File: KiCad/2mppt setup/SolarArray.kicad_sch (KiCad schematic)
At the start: 4 parts

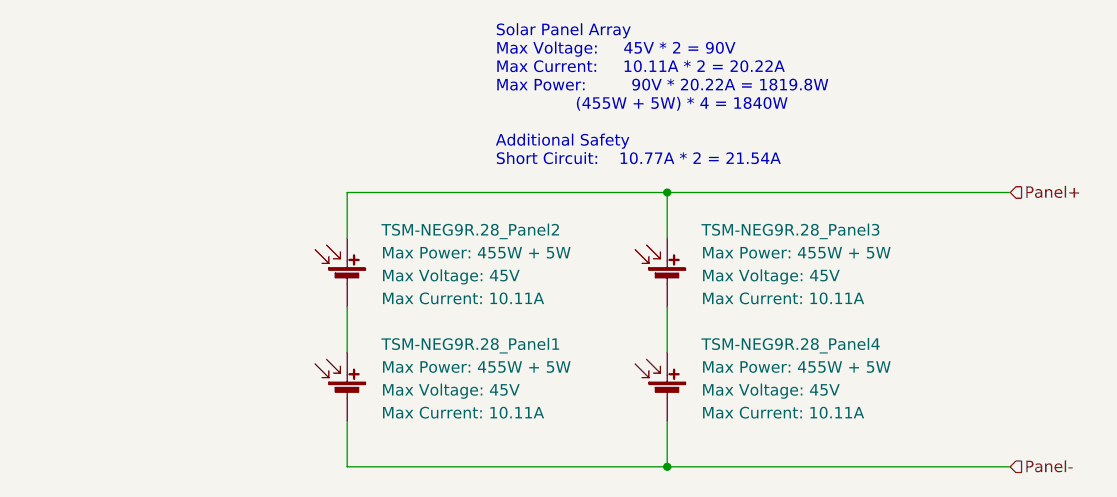
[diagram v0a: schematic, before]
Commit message: exclude text from sim
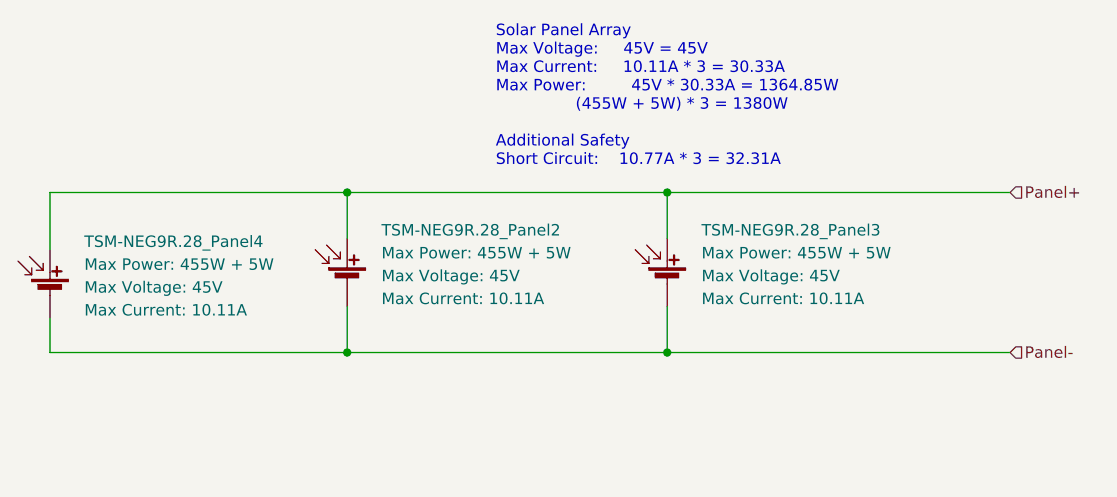
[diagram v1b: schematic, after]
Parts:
- removed TSM-NEG9R.28_Panel1: 455W, symbol Proa:Solar_Cell
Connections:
- net Panel+: now also TSM-NEG9R.28_Panel4.1 (+)
- net Panel-: now also TSM-NEG9R.28_Panel2.2 (-), TSM-NEG9R.28_Panel3.2 (-)
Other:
- note added: "Solar Panel Array Max Voltage: 45V = 45V Max Current: 10.11A * 3 = 30.33A Max Power: 45V * 30.33A = 1364.85W (455W + 5W) * 3 = 1380W Additional Safety Short Circuit: 10.77A * 3 = 32.31A"
- note removed: "Solar Panel Array Max Voltage: 45V * 2 = 90V Max Current: 10.11A * 2 = 20.22A Max Power: 90V * 20.22A = 1819.8W (455W + 5W) * 4 = 1840W Additional Safety Short Circuit: 10.77A * 2 = 21.54A"
- moved on the sheet: TSM-NEG9R.28_Panel4
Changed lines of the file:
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@@
 	(generator_version "9.0")
 	(paper "A4")
-	(text "Solar Panel Array\nMax Voltage: 	45V * 2 = 90V\nMax Current: 	10.11A * 2 = 20.22A\nMax Power: 		90V * 20.22A = 1819.8W\n				(455W + 5W) * 4 = 1840W\n\nAdditional Safety\nShort Circuit:	10.77A * 2 = 21.54A"
-		(exclude_from_sim no)
+	(text "Solar Panel Array\nMax Voltage: 	45V = 45V\nMax Current: 	10.11A * 3 = 30.33A\nMax Power: 		45V * 30.33A = 1364.85W\n				(455W + 5W) * 3 = 1380W\n\nAdditional Safety\nShort Circuit:	10.77A * 3 = 32.31A\n"
+		(exclude_from_sim yes)
 		(at 120.65 54.102 0)
 		(effects
@@
 	)
 	(junction
+		(at 139.7 82.55)
+		(diameter 0)
+		(color 0 0 0 0)
+	)
+	(junction
+		(at 104.14 82.55)
+		(diameter 0)
+		(color 0 0 0 0)
+	)
+	(junction
+		(at 104.14 64.77)
+		(diameter 0)
+		(color 0 0 0 0)
+	)
+	(junction
 		(at 139.7 64.77)
 		(diameter 0)
 		(color 0 0 0 0)
 	)
-	(junction
-		(at 139.7 95.25)
-		(diameter 0)
-		(color 0 0 0 0)
-	)
-	(wire
-		(pts
-			(xy 104.14 95.25) (xy 139.7 95.25)
-		)
-		(stroke
-			(width 0)
-			(type default)
-		)
-	)
-	(wire
-		(pts
-			(xy 104.14 90.17) (xy 104.14 95.25)
+	(wire
+		(pts
+			(xy 71.12 71.12) (xy 71.12 64.77)
 		)
 		(stroke
@@
 	(wire
 		(pts
-			(xy 139.7 95.25) (xy 177.8 95.25)
+			(xy 71.12 64.77) (xy 104.14 64.77)
 		)
 		(stroke
@@
 	(wire
 		(pts
+			(xy 139.7 82.55) (xy 177.8 82.55)
+		)
+		(stroke
+			(width 0)
+			(type default)
+		)
+	)
+	(wire
+		(pts
+			(xy 71.12 78.74) (xy 71.12 82.55)
+		)
+		(stroke
+			(width 0)
+			(type default)
+		)
+	)
+	(wire
+		(pts
 			(xy 104.14 64.77) (xy 104.14 69.85)
 		)
@@
 	(wire
 		(pts
+			(xy 71.12 82.55) (xy 104.14 82.55)
+		)
+		(stroke
+			(width 0)
+			(type default)
+		)
+	)
+	(wire
+		(pts
 			(xy 104.14 77.47) (xy 104.14 82.55)
 		)
@@
 	(wire
 		(pts
-			(xy 139.7 95.25) (xy 139.7 90.17)
+			(xy 104.14 82.55) (xy 139.7 82.55)
 		)
 		(stroke
@@
 	(hierarchical_label "Panel-"
 		(shape input)
-		(at 177.8 95.25 0)
+		(at 177.8 82.55 0)
 		(effects
 			(font
@@
 	(symbol
 		(lib_id "Proa:Solar_Cell")
-		(at 139.7 87.63 0)
+		(at 71.12 76.2 0)
 		(unit 1)
 		(exclude_from_sim no)
@@
 		(fields_autoplaced yes)
 		(property "Reference" "TSM-NEG9R.28_Panel4"
-			(at 143.51 81.6609 0)
+			(at 74.93 70.2309 0)
 			(effects
 				(font
@@
 		)
 		(property "Value" "455W"
-			(at 143.51 86.7409 0)
+			(at 74.93 75.3109 0)
 			(effects
 				(font
@@
 		)
 		(property "Footprint" ""
-			(at 139.7 86.106 90)
+			(at 71.12 74.676 90)
 			(effects
 				(font
@@
 		)
 		(property "Datasheet" "~"
-			(at 139.7 86.106 90)
+			(at 71.12 74.676 90)
 			(effects
 				(font
@@
 		)
 		(property "Description" "Single solar cell"
-			(at 139.7 87.63 0)
+			(at 71.12 76.2 0)
 			(effects
 				(font
@@
 		)
 		(property "Max Power" "455W + 5W"
-			(at 143.51 84.2009 0)
+			(at 74.93 72.7709 0)
 			(show_name yes)
 			(effects
@@
 		)
 		(property "Max Voltage" "45V"
-			(at 143.51 86.7409 0)
+			(at 74.93 75.3109 0)
 			(show_name yes)
 			(effects
@@
 		)
 		(property "Max Current" "10.11A"
-			(at 143.51 89.2809 0)
+			(at 74.93 77.8509 0)
 			(show_name yes)
 			(effects
@@
 				)
 				(path "/a5748c52-e651-4363-96d3-c9fc6357a5ef/cebab42b-7f95-493f-a532-afa591df43ce"
-					(reference "TSM-NEG9R.28_Panel7")
+					(reference "TSM-NEG9R.28_Panel1")
 					(unit 1)
 				)
@@
 					(unit 1)
 				)
-			)
-		)
-	)
-	(symbol
-		(lib_id "Proa:Solar_Cell")
-		(at 104.14 87.63 0)
-		(unit 1)
-		(exclude_from_sim no)
-		(in_bom yes)
-		(on_board yes)
-		(dnp no)
-		(fields_autoplaced yes)
-		(property "Reference" "TSM-NEG9R.28_Panel1"
-			(at 107.95 81.6609 0)
-			(effects
-				(font
-					(size 1.27 1.27)
-				)
-				(justify left)
-			)
-		)
-		(property "Value" "455W"
-			(at 107.95 86.7409 0)
-			(effects
-				(font
-					(size 1.27 1.27)
-				)
-				(justify left)
-				(hide yes)
-			)
-		)
-		(property "Footprint" ""
-			(at 104.14 86.106 90)
-			(effects
-				(font
-					(size 1.27 1.27)
-				)
-				(hide yes)
-			)
-		)
-		(property "Datasheet" "~"
-			(at 104.14 86.106 90)
-			(effects
-				(font
-					(size 1.27 1.27)
-				)
-				(hide yes)
-			)
-		)
-		(property "Description" "Single solar cell"
-			(at 104.14 87.63 0)
-			(effects
-				(font
-					(size 1.27 1.27)
-				)
-				(hide yes)
-			)
-		)
-		(property "Max Power" "455W + 5W"
-			(at 107.95 84.2009 0)
-			(show_name yes)
-			(effects
-				(font
-					(size 1.27 1.27)
-				)
-				(justify left)
-			)
-		)
-		(property "Max Voltage" "45V"
-			(at 107.95 86.7409 0)
-			(show_name yes)
-			(effects
-				(font
-					(size 1.27 1.27)
-				)
-				(justify left)
-			)
-		)
-		(property "Max Current" "10.11A"
-			(at 107.95 89.2809 0)
-			(show_name yes)
-			(effects
-				(font
-					(size 1.27 1.27)
-				)
-				(justify left)
-			)
-		)
-		(pin "2"
-		)
-		(pin "1"
-		)
-		(instances
-			(project "2mppt setup"
-				(path "/a5748c52-e651-4363-96d3-c9fc6357a5ef/883227c1-d3ab-479d-b77c-fbb903e126a8"
-					(reference "TSM-NEG9R.28_Panel1")
-					(unit 1)
-				)
-				(path "/a5748c52-e651-4363-96d3-c9fc6357a5ef/cebab42b-7f95-493f-a532-afa591df43ce"
-					(reference "TSM-NEG9R.28_Panel5")
-					(unit 1)
-				)
